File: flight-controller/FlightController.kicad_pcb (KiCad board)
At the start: 2 copper layers, 40 x 37 mm, 30 parts, among them J1 MSD-4-A, J2 Conn_01x03_Pin, J3 Conn_01x03_Pin, J4 Conn_01x03_Pin, J5 Conn_01x03_Pin, J6 USB4215-03-A_REVA, J7 Conn_01x03_Pin, J8 Conn_01x03_Pin, U1 ESP32-S3-WROOM-1, U2 TPS629210DRLR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

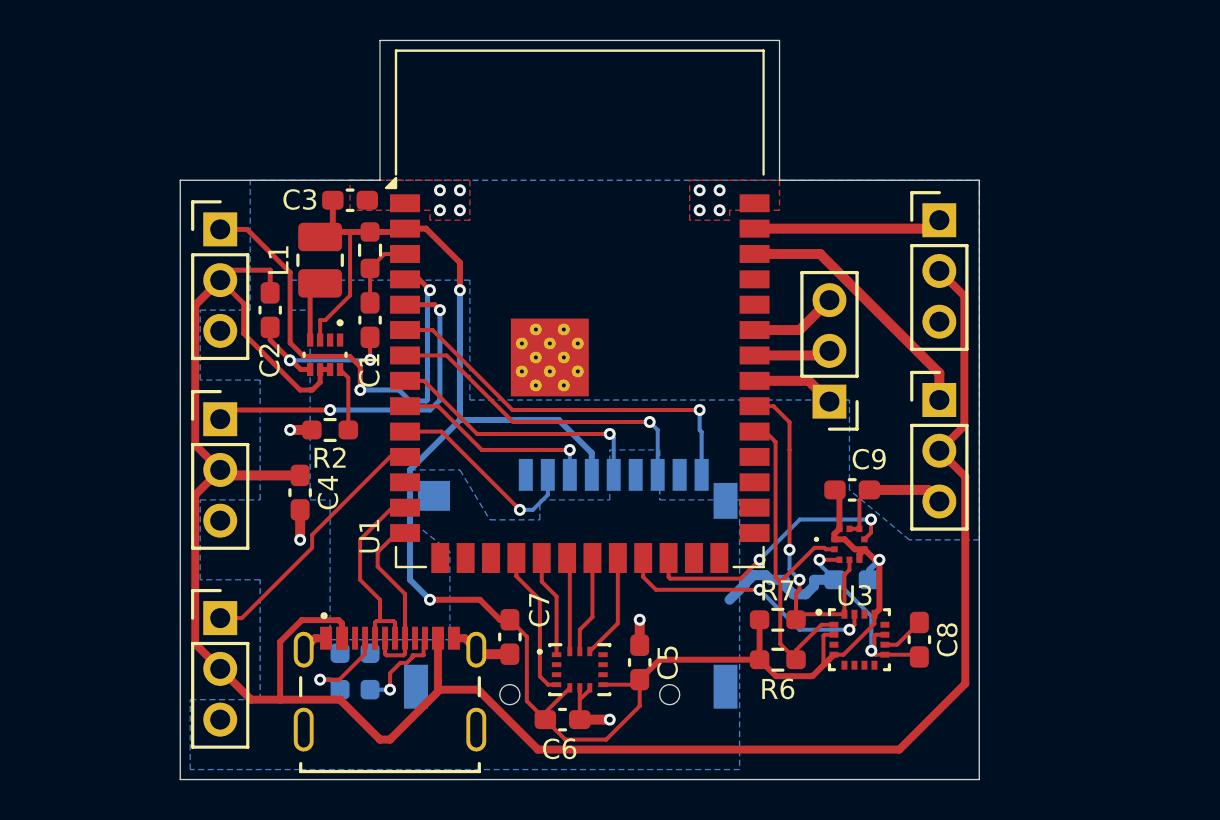
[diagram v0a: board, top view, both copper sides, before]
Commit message: add uart header
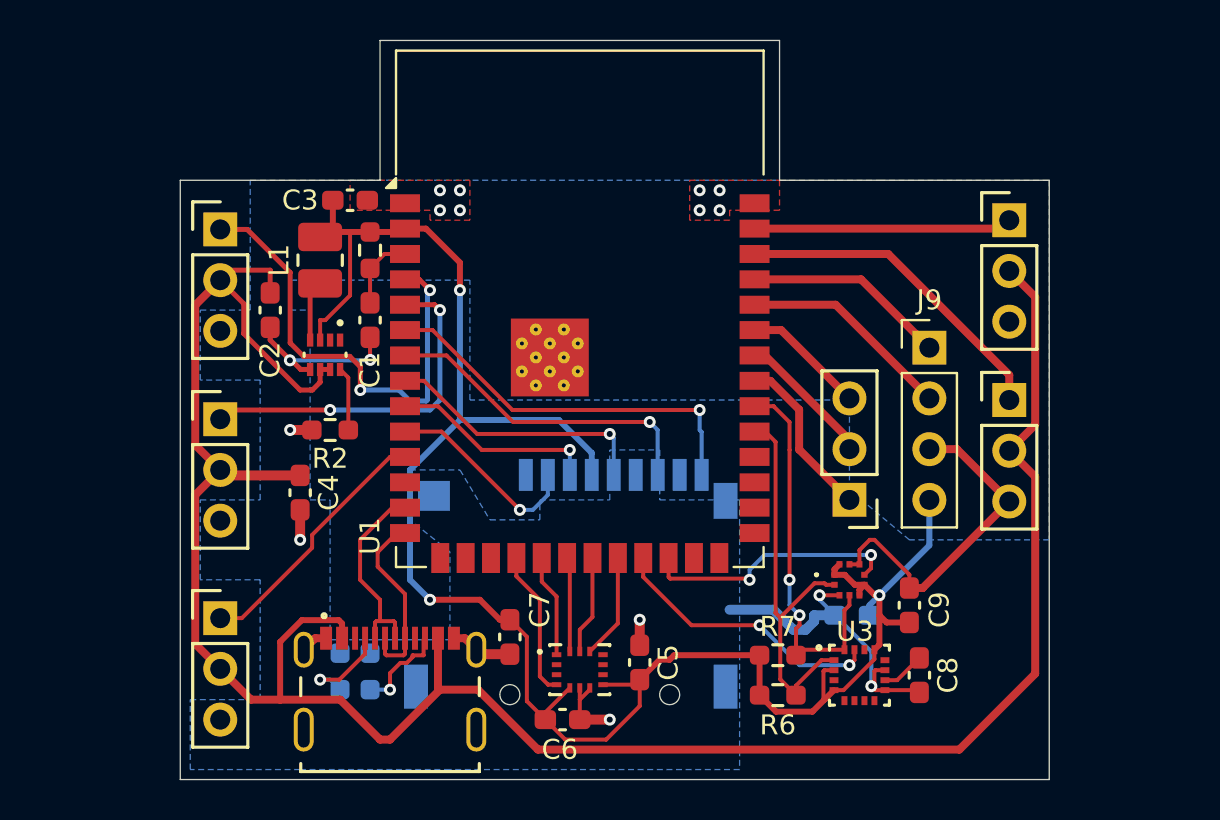
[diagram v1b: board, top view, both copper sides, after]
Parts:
- added J9: Conn_01x04_Pin, Connector_PinHeader_2.54mm:PinHeader_1x04_P2.54mm_Vertical, F.Cu at (127.5, 58.4)
- moved C9 6.45 mm to (126.5, 71.3), turned to -90 degrees
- moved J8 5.02 mm to (123.5, 66.0)
- moved J4 3.50 mm to (131.5, 52.0)
- moved J5 3.50 mm to (131.5, 61.0)
- moved C10 1.78 mm to (123.6, 71.8)
- moved C8 1.78 mm to (127.0, 74.8)
- moved R6 1.78 mm to (119.9, 75.8)
- moved R7 1.78 mm to (119.9, 73.8)
- moved U3 1.78 mm to (124.0, 74.8)
- moved U5 1.78 mm to (123.5, 70.0)
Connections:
- U1 pad 36: unconnected-(U1-RXD0-Pad36) -> ESP_RX
- U1 pad 37: unconnected-(U1-TXD0-Pad37) -> ESP_TX
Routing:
- net ESP_RX: track 0.00 -> 10.7 mm
- net ESP_TX: track 0.00 -> 10.2 mm
- net GND: track 44.8 -> 54.9 mm
- net +3.3V: track 91.0 -> 96.5 mm
- net IO40: track 4.18 -> 8.39 mm
- net MOTOR3_PWM: track 9.42 -> 12.9 mm
- net MOTOR4_PWM: track 13.1 -> 16.5 mm
- net +5V: track 113.5 -> 116.7 mm
- net IO41: track 3.85 -> 6.96 mm
- net I2C_SCL: track 18.9 -> 20.8 mm
- net IO42: track 4.37 -> 6.17 mm
- net I2C_SDA: track 17.6 -> 19.4 mm
- net MAG_INT: track 13.2 -> 14.0 mm
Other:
- board size 40 x 37 mm -> 43.5 x 37 mm

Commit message: add mounting holes
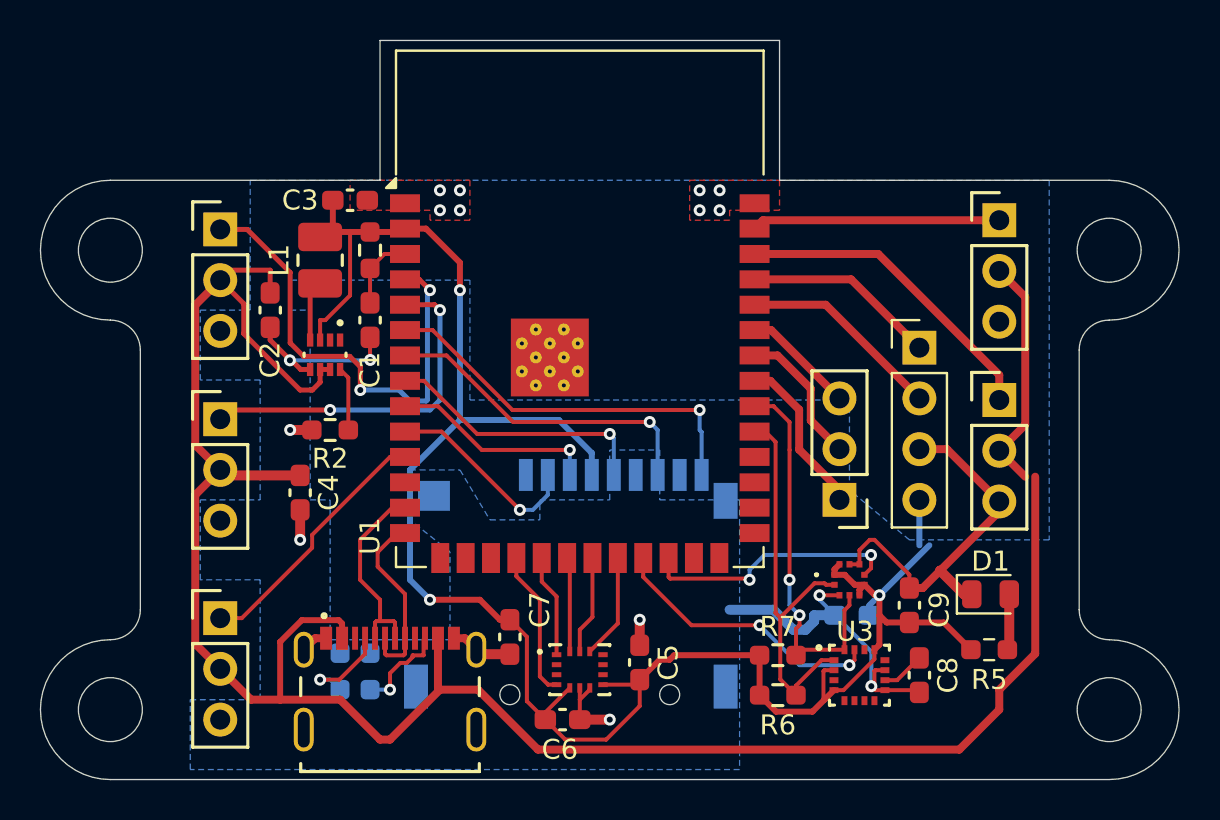
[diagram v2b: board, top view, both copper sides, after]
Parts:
- added D1: LED, LED_SMD:LED_0805_2012Metric, F.Cu at (130.6, 70.7)
- added H1: MountingHole, MountingHole:MountingHole_3.2mm_M3, F.Cu at (86.5, 53.5)
- added H2: MountingHole, MountingHole:MountingHole_3.2mm_M3, F.Cu at (86.5, 76.5)
- added H3: MountingHole, MountingHole:MountingHole_3.2mm_M3, F.Cu at (136.5, 53.5)
- added H4: MountingHole, MountingHole:MountingHole_3.2mm_M3, F.Cu at (136.5, 76.5)
- added R5: 1k, Resistor_SMD:R_0603_1608Metric_Pad0.98x0.95mm_HandSolder, F.Cu at (130.5, 73.5)
- moved J4 0.50 mm to (131.0, 52.0)
- moved J5 0.50 mm to (131.0, 61.0)
- moved J8 0.50 mm to (123.0, 66.0)
- moved J9 0.50 mm to (127.0, 58.4)
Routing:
- net +3.3V: track 96.5 -> 100.1 mm
- net Net-(D1-A): track 0.00 -> 2.81 mm
- net GND: track 54.9 -> 57.0 mm
- net IO41: track 6.96 -> 7.58 mm
- net MOTOR4_PWM: track 16.5 -> 16.0 mm
- net IO42: track 6.17 -> 5.67 mm
- net ESP_TX: track 10.2 -> 9.67 mm
- net ESP_RX: track 10.7 -> 10.2 mm
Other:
- board size 43.5 x 37 mm -> 57 x 37 mm
